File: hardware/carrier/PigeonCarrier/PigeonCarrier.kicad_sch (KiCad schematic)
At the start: 0 parts

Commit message: added CM5
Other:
- added sheet CM5 (CM5.kicad_sch)
- added sheet Cameras (Cameras.kicad_sch)
- added sheet Regulators (Regulators.kicad_sch)
- added sheet Sensors (Sensors.kicad_sch)
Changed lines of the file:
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@@
 	(generator_version "10.0")
 	(paper "A4")
+	(sheet
+		(at 55.88 75.565)
+		(size 33.655 25.4)
+		(exclude_from_sim no)
+		(in_bom yes)
+		(on_board yes)
+		(dnp no)
+		(fields_autoplaced yes)
+		(stroke
+			(width 0.1524)
+			(type solid)
+		)
+		(fill
+			(color 0 0 0 0)
+		)
+		(property "Sheetname" "Regulators"
+			(at 55.88 74.8534 0)
+			(show_name no)
+			(do_not_autoplace no)
+			(effects
+				(font
+					(size 1.27 1.27)
+				)
+				(justify left bottom)
+			)
+		)
+		(property "Sheetfile" "Regulators.kicad_sch"
+			(at 55.88 101.5496 0)
+			(show_name no)
+			(do_not_autoplace no)
+			(effects
+				(font
+					(size 1.27 1.27)
+				)
+				(justify left top)
+			)
+		)
+		(instances
+			(project "PigeonCarrier"
+				(path "/6c8da0f4-34cf-43b9-a25b-857048b8016b"
+					(page "3")
+				)
+			)
+		)
+	)
+	(sheet
+		(at 123.825 85.09)
+		(size 55.245 53.975)
+		(exclude_from_sim no)
+		(in_bom yes)
+		(on_board yes)
+		(dnp no)
+		(fields_autoplaced yes)
+		(stroke
+			(width 0.1524)
+			(type solid)
+		)
+		(fill
+			(color 0 0 0 0)
+		)
+		(property "Sheetname" "CM5"
+			(at 123.825 84.3784 0)
+			(show_name no)
+			(do_not_autoplace no)
+			(effects
+				(font
+					(size 1.27 1.27)
+				)
+				(justify left bottom)
+			)
+		)
+		(property "Sheetfile" "CM5.kicad_sch"
+			(at 123.825 139.6496 0)
+			(show_name no)
+			(do_not_autoplace no)
+			(effects
+				(font
+					(size 1.27 1.27)
+				)
+				(justify left top)
+			)
+		)
+		(instances
+			(project "PigeonCarrier"
+				(path "/6c8da0f4-34cf-43b9-a25b-857048b8016b"
+					(page "2")
+				)
+			)
+		)
+	)
+	(sheet
+		(at 55.88 120.65)
+		(size 34.29 26.035)
+		(exclude_from_sim no)
+		(in_bom yes)
+		(on_board yes)
+		(dnp no)
+		(fields_autoplaced yes)
+		(stroke
+			(width 0.1524)
+			(type solid)
+		)
+		(fill
+			(color 0 0 0 0)
+		)
+		(property "Sheetname" "Cameras"
+			(at 55.88 119.9384 0)
+			(show_name no)
+			(do_not_autoplace no)
+			(effects
+				(font
+					(size 1.27 1.27)
+				)
+				(justify left bottom)
+			)
+		)
+		(property "Sheetfile" "Cameras.kicad_sch"
+			(at 55.88 147.2696 0)
+			(show_name no)
+			(do_not_autoplace no)
+			(effects
+				(font
+					(size 1.27 1.27)
+				)
+				(justify left top)
+			)
+		)
+		(instances
+			(project "PigeonCarrier"
+				(path "/6c8da0f4-34cf-43b9-a25b-857048b8016b"
+					(page "4")
+				)
+			)
+		)
+	)
+	(sheet
+		(at 126.365 47.625)
+		(size 47.625 17.145)
+		(exclude_from_sim no)
+		(in_bom yes)
+		(on_board yes)
+		(dnp no)
+		(fields_autoplaced yes)
+		(stroke
+			(width 0.1524)
+			(type solid)
+		)
+		(fill
+			(color 0 0 0 0)
+		)
+		(property "Sheetname" "Sensors"
+			(at 126.365 46.9134 0)
+			(show_name no)
+			(do_not_autoplace no)
+			(effects
+				(font
+					(size 1.27 1.27)
+				)
+				(justify left bottom)
+			)
+		)
+		(property "Sheetfile" "Sensors.kicad_sch"
+			(at 126.365 65.3546 0)
+			(show_name no)
+			(do_not_autoplace no)
+			(effects
+				(font
+					(size 1.27 1.27)
+				)
+				(justify left top)
+			)
+		)
+		(instances
+			(project "PigeonCarrier"
+				(path "/6c8da0f4-34cf-43b9-a25b-857048b8016b"
+					(page "5")
+				)
+			)
+		)
+	)
 	(sheet_instances
 		(path "/"

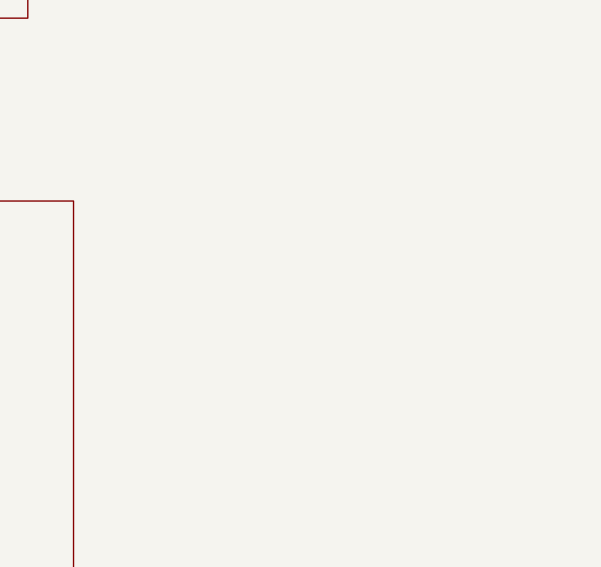
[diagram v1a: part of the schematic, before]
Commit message: add Ethernet sheet
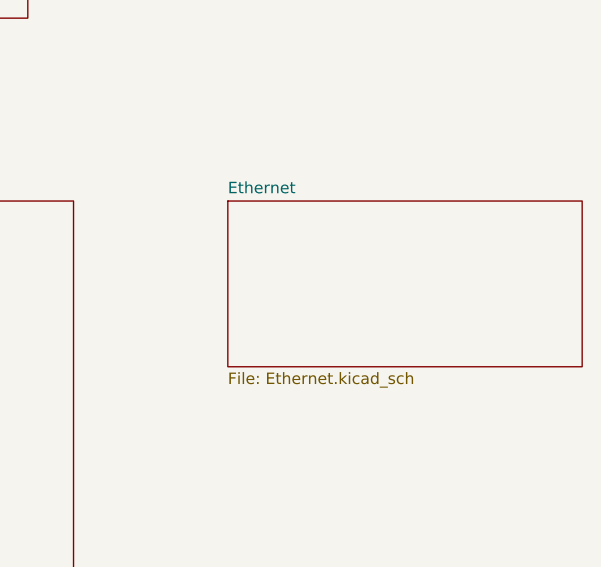
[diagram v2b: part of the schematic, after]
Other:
- added sheet Ethernet (Ethernet.kicad_sch)
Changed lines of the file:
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@@
+	)
+	(sheet
+		(at 196.215 85.09)
+		(size 39.37 18.415)
+		(exclude_from_sim no)
+		(in_bom yes)
+		(on_board yes)
+		(dnp no)
+		(fields_autoplaced yes)
+		(stroke
+			(width 0.1524)
+			(type solid)
+		)
+		(fill
+			(color 0 0 0 0)
+		)
+		(property "Sheetname" "Ethernet"
+			(at 196.215 84.3784 0)
+			(show_name no)
+			(do_not_autoplace no)
+			(effects
+				(font
+					(size 1.27 1.27)
+				)
+				(justify left bottom)
+			)
+		)
+		(property "Sheetfile" "Ethernet.kicad_sch"
+			(at 196.215 104.0896 0)
+			(show_name no)
+			(do_not_autoplace no)
+			(effects
+				(font
+					(size 1.27 1.27)
+				)
+				(justify left top)
+			)
+		)
+		(instances
+			(project "PigeonCarrier"
+				(path "/6c8da0f4-34cf-43b9-a25b-857048b8016b"
+					(page "6")
+				)
+			)
+		)
 	)
 	(sheet

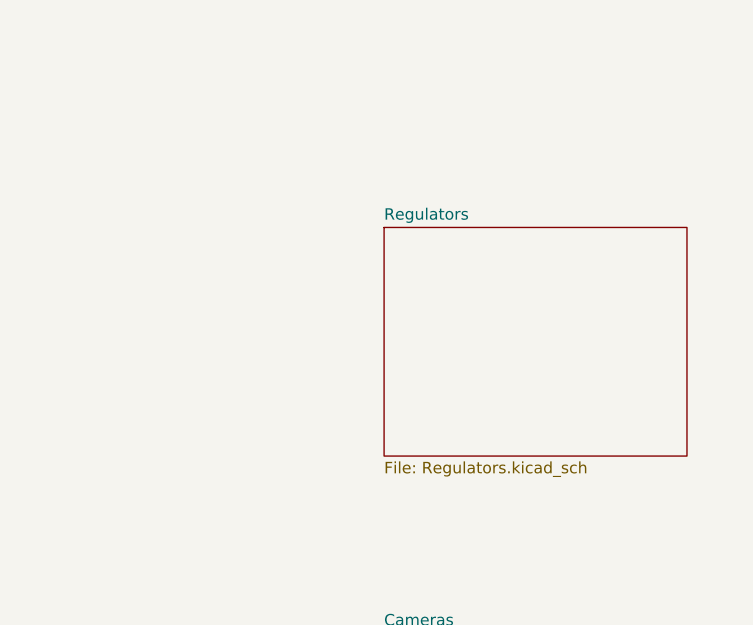
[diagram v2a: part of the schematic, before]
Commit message: shortned readmes + start of power stuff
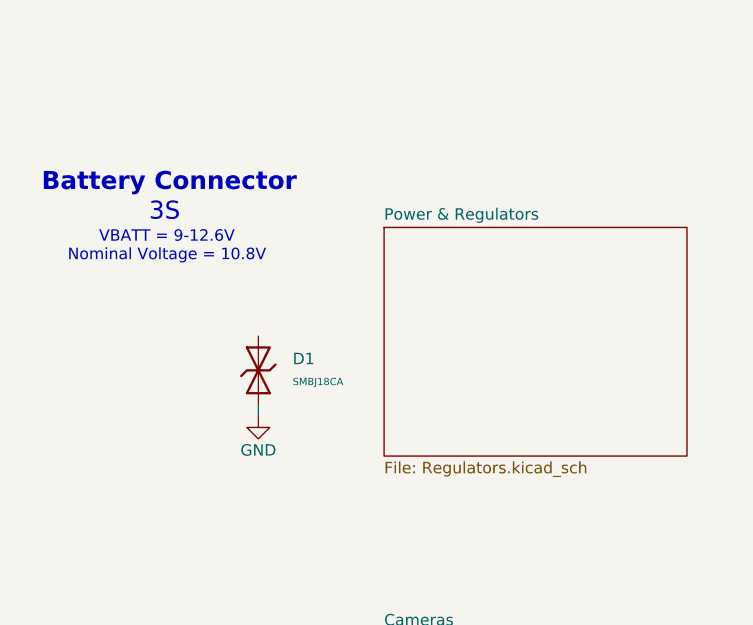
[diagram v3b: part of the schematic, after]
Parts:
- added D1: SMBJ18CA, PCM_JLCPCB:D_SMB, symbol PCM_JLCPCB-Diodes:TVS-Bi,SMBJ18CA
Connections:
- new net GND: D1.1
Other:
- sheet Regulators renamed Power & Regulators
- note added: "3S"
- note added: "Battery Connector"
- note added: "VBATT = 9-12.6V Nominal Voltage = 10.8V"

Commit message: carrier progress
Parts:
- added J3: BATT CONN, Connector_AMASS:AMASS_XT60PW-M_1x02_P7.20mm_Horizontal, symbol Connector:Conn_01x02_Pin
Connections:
- net GND: now also J3.1 (Pin_1)
- net Power & Regulators/VBAT_RAW: now reaches D1.2
- net Power & Regulators/VBAT_RAW: now also J3.2 (Pin_2)
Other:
- added sheet Yapogee_Interface (yapogee.kicad_sch)
- sheet Power & Regulators ports: added 1V8_CAM_EN, 4V_CAM_EN, SCL_0, SDA_0, VBAT_RAW; removed none
- note added: "18V TVS"
- note added: "VBATT = 8.1-12.6V Nominal Voltage = 10.8V"
- note added: "XT-60"
- note removed: "VBATT = 9-12.6V Nominal Voltage = 10.8V"
- moved on the sheet: D1

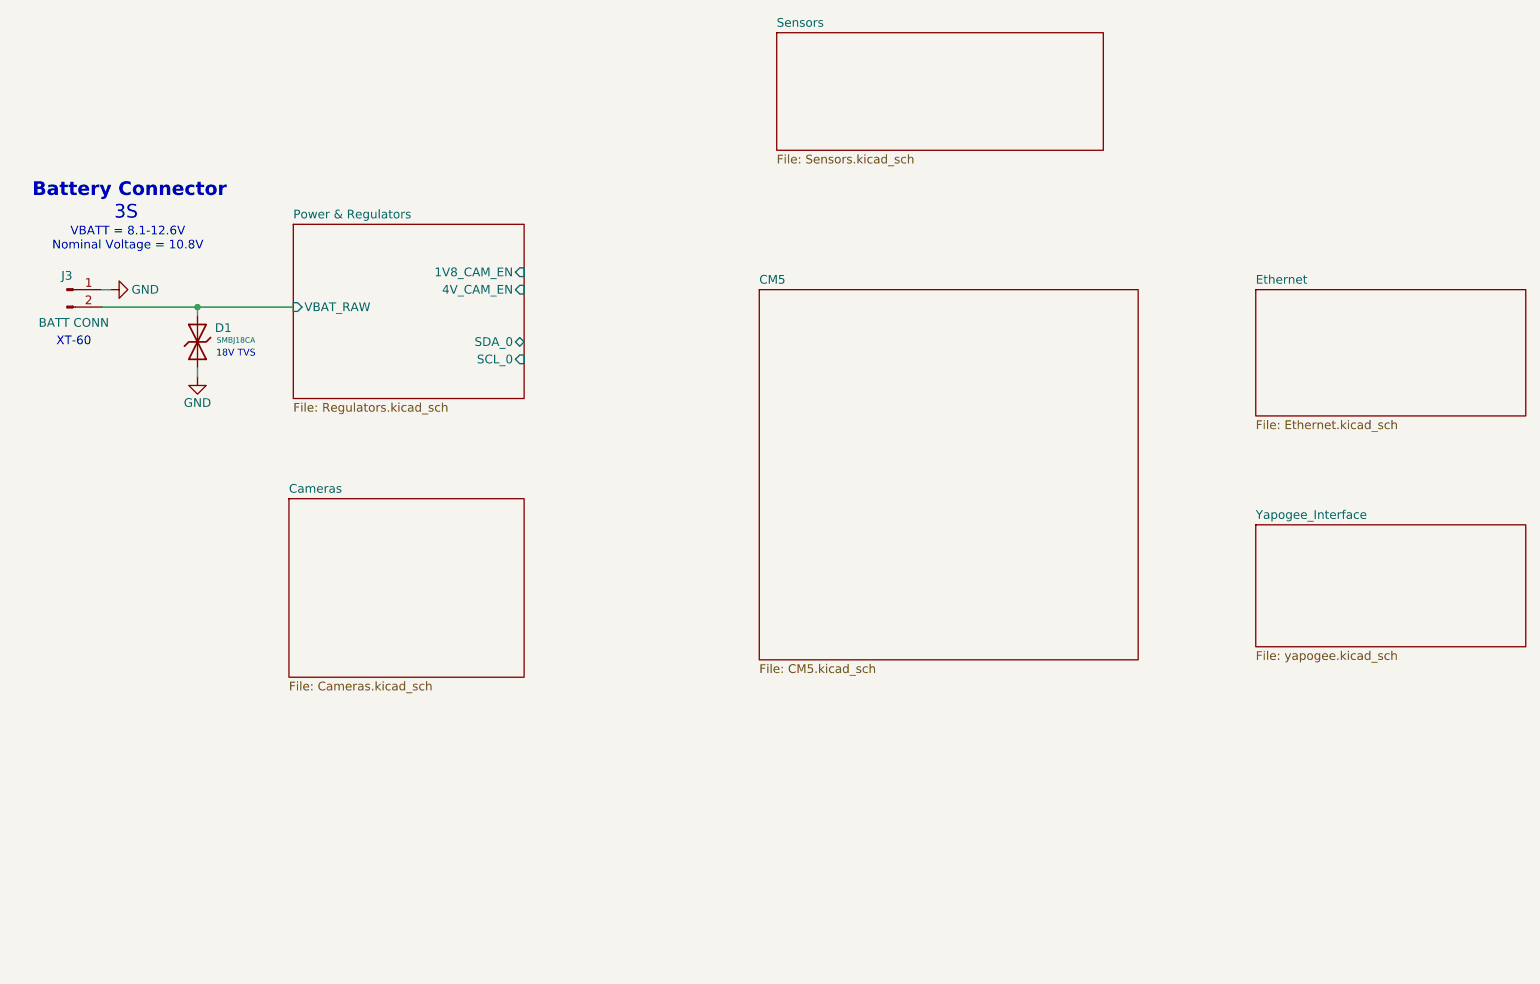
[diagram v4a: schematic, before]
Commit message: Update carrier schematics, parts library, and JLC rules
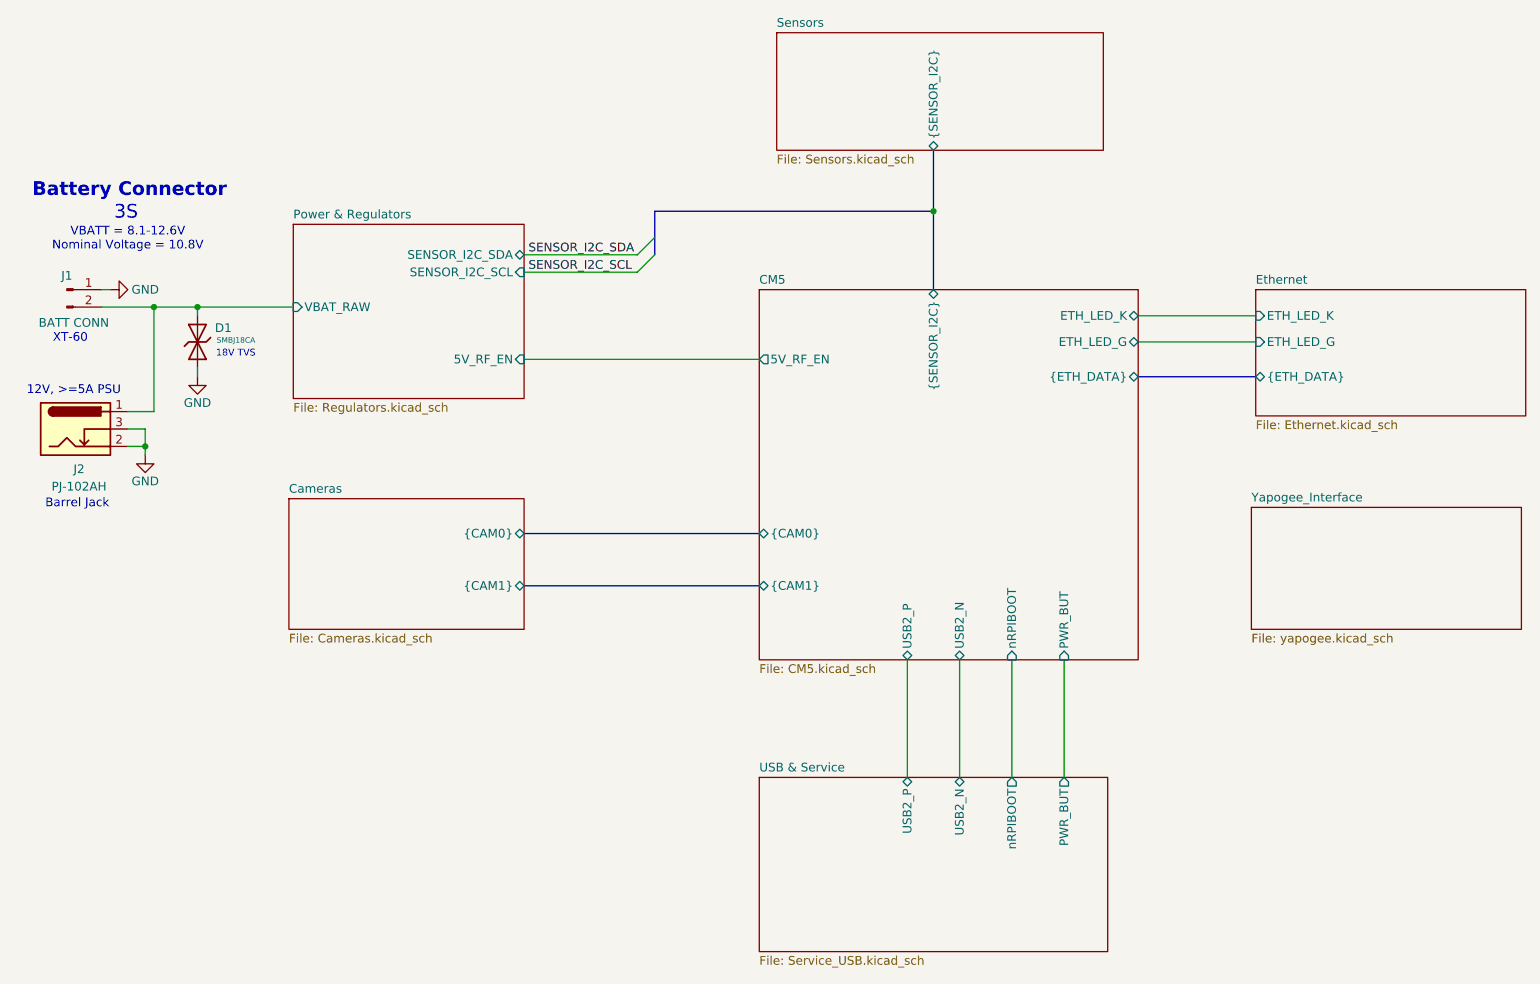
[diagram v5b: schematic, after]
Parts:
- added J2: PJ-102AH, PigeonVision:SameSky_PJ-102AH_Horizontal, symbol PigeonVision:PJ-102AH
- renumbered J3 to J1
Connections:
- net GND: now also J2.2 (Sleeve), J2.3 (Sleeve_Shunt)
- net Power & Regulators/VBAT_RAW: now also J2.1 (Center)
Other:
- added sheet USB & Service (Service_USB.kicad_sch)
- sheet CM5 ports: added 5V_RF_EN, ETH_LED_G, ETH_LED_K, PWR_BUT, USB2_N, USB2_P, nRPIBOOT, {CAM0}, {CAM1}, {ETH_DATA}, {SENSOR_I2C}; removed none
- sheet Cameras ports: added {CAM0}, {CAM1}; removed none
- sheet Ethernet ports: added ETH_LED_G, ETH_LED_K, {ETH_DATA}; removed none
- sheet Power & Regulators ports: added 5V_RF_EN, SENSOR_I2C_SCL, SENSOR_I2C_SDA; removed 1V8_CAM_EN, 4V_CAM_EN, SCL_0, SDA_0
- sheet Sensors ports: added {SENSOR_I2C}; removed none
- note added: "12V, >=5A PSU"
- note added: "Barrel Jack"

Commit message: finished rough layout
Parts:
- D1: MPN (none) -> SMBJ18CA
- J1: MPN (none) -> XT60PW-M; Manufacturer (none) -> AMASS
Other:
- sheet CM5 ports: added ETH_LED_Y; removed ETH_LED_K
- sheet Ethernet ports: added ETH_LED_Y; removed ETH_LED_K
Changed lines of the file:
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@@
 	)
 	(bus_entry
-		(at 106.045 80.01)
+		(at 106.68 80.01)
 		(size 2.54 -2.54)
 		(stroke
@@
 	)
 	(bus_entry
-		(at 106.045 82.55)
+		(at 106.68 82.55)
 		(size 2.54 -2.54)
 		(stroke
@@
 	(wire
 		(pts
-			(xy 89.535 80.01) (xy 106.045 80.01)
+			(xy 89.535 80.01) (xy 106.68 80.01)
 		)
 		(stroke
@@
 	(wire
 		(pts
-			(xy 89.535 82.55) (xy 106.045 82.55)
+			(xy 89.535 82.55) (xy 106.68 82.55)
 		)
 		(stroke
@@
 	(bus
 		(pts
-			(xy 108.585 73.66) (xy 108.585 80.01)
+			(xy 109.22 73.66) (xy 109.22 80.01)
 		)
 		(stroke
@@
 	(bus
 		(pts
-			(xy 108.585 73.66) (xy 149.225 73.66)
+			(xy 109.22 73.66) (xy 149.225 73.66)
 		)
 		(stroke
@@
 	)
 	(label "SENSOR_I2C_SDA"
-		(at 90.17 80.01 0)
+		(at 90.805 80.01 0)
 		(effects
 			(font
@@
 	)
 	(label "SENSOR_I2C_SCL"
-		(at 90.17 82.55 0)
+		(at 90.805 82.55 0)
 		(effects
 			(font
@@
 			)
 		)
+		(property "MPN" "XT60PW-M"
+			(at 22.86 85.09 0)
+			(hide yes)
+			(show_name no)
+			(do_not_autoplace no)
+			(effects
+				(font
+					(size 1.27 1.27)
+				)
+			)
+		)
+		(property "Manufacturer" "AMASS"
+			(at 22.86 85.09 0)
+			(hide yes)
+			(show_name no)
+			(do_not_autoplace no)
+			(effects
+				(font
+					(size 1.27 1.27)
+				)
+			)
+		)
 		(pin "2"
 		)
@@
 			)
 		)
+		(property "MPN" "SMBJ18CA"
+			(at 41.91 92.71 0)
+			(hide yes)
+			(show_name no)
+			(do_not_autoplace no)
+			(effects
+				(font
+					(size 1.27 1.27)
+				)
+			)
+		)
 		(pin "1"
 		)
@@
 			)
 		)
-		(pin "ETH_LED_K" bidirectional
+		(pin "ETH_LED_Y" bidirectional
 			(at 179.07 88.9 0)
 			(effects
@@
 			)
 		)
-		(pin "ETH_LED_K" input
+		(pin "ETH_LED_Y" input
 			(at 196.215 88.9 180)
 			(effects

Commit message: Update carrier placement and vertical connector libraries
Save the latest component placements and mechanical mounting changes. Include the vertical XT60/XT30 and camera connector symbols, footprints, redistributable CAD, licenses and documentation. Keep local-only vendor models ignored.

Validation: ERC has zero findings. Native KiCad loading and netlist comparison confirm all 152 schematic components and 681 numbered pads agree. Full DRC could not complete because the KiCad CLI aborted in this environment.
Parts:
- J1: footprint Connector_AMASS:AMASS_XT60PW-M_1x02_P7.20mm_Horizontal -> PigeonVision:AMASS_XT60PB-M_1x02_P7.20mm_Vertical_2025; symbol Connector:Conn_01x02_Pin -> PigeonVision:AMASS_XT60PB_M30_G_Y; LCSC C98732 -> C19268037; LCSC Part # (none) -> C19268037; MPN XT60PW-M -> XT60PB-M30.G.Y; Sourcing note (none) -> LCSC short MPN XT60PB-M.G.Y;manufacturer2025V0 full SKU XT6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
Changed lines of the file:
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@@
 	)
 	(symbol
-		(lib_id "Connector:Conn_01x02_Pin")
+		(lib_id "PigeonVision:AMASS_XT60PB_M30_G_Y")
 		(at 22.86 85.09 0)
 		(unit 1)
@@
 			)
 		)
-		(property "Footprint" "Connector_AMASS:AMASS_XT60PW-M_1x02_P7.20mm_Horizontal"
+		(property "Footprint" "PigeonVision:AMASS_XT60PB-M_1x02_P7.20mm_Vertical_2025"
 			(at 22.86 85.09 0)
 			(hide yes)
@@
 			)
 		)
-		(property "Datasheet" ""
+		(property "Datasheet" "https://www.china-amass.net/uploads/62.XT60PB-M-SPEC-2025V0.pdf"
 			(at 22.86 85.09 0)
 			(hide yes)
@@
 			)
 		)
-		(property "Description" "Generic connector, single row, 01x02, script generated"
+		(property "Description" "AMASS XT60PB-M30.G.Y vertical PCB male;1 negative/keyed side,2 positive/flat side;7.20mm pitch;2025V0 finished holes4.6+0.1/-0mm. Enabled detailed CalSTAR-based local planning STEP has7.2mm contact pitch and3mm tails; exact factory PCB tail geometry unverified. Not manufacturer CAD."
 			(at 22.86 85.09 0)
 			(hide yes)
@@
 			)
 		)
-		(property "LCSC" "C98732"
+		(property "LCSC" "C19268037"
 			(at 22.86 85.09 0)
 			(hide yes)
@@
 			)
 		)
-		(property "MPN" "XT60PW-M"
+		(property "MPN" "XT60PB-M30.G.Y"
 			(at 22.86 85.09 0)
 			(hide yes)
@@
 			)
 		)
-	)
+	(property "LCSC Part #" "C19268037" (at 22.86 85.09 0) (hide yes) (effects (font (size 1.27 1.27))))
+	(property "Sourcing note" "LCSC short MPN XT60PB-M.G.Y;manufacturer2025V0 full SKU XT60PB-M30.G.Y. JLC assembly inventory not verified." (at 22.86 85.09 0) (hide yes) (effects (font (size 1.27 1.27))))
+	(mirror y)
+)
 	(symbol
 		(lib_id "PCM_JLCPCB-Diodes:TVS-Bi,SMBJ18CA")
